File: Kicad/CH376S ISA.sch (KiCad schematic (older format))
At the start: 29 parts, among them J1 Bus_ISA_8bit, J2 ROM CS, J3 Conn_02x04_Odd_Even, U1 CH376, U13 74LS138, U14 74LS138, U15 74LS138, U2 LM1117-3.3, U3 74LS139, U4 74LS138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

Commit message: first draft done
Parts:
- removed C3: 0.1uF, Capacitor_THT:C_Disc_D4.3mm_W1.9mm_P5.00mm, symbol pspice:CAP
- removed J3: Conn_02x04_Odd_Even, Connector_PinHeader_2.54mm:PinHeader_2x04_P2.54mm_Vertical, symbol Connector_Generic:Conn_02x04_Odd_Even
- removed U3: 74LS139, Package_DIP:DIP-16_W7.62mm, symbol 74xx:74LS139
- removed U6: 28C64, Package_DIP:DIP-28_W15.24mm, symbol Memory_EPROM:27C64
- added U3: 28C256, Package_DIP:DIP-28_W15.24mm, symbol Memory_EEPROM:28C256
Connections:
- net IO_00EX is gone; now on net CH376CS: U15.7 (O7)
- net 5+: now also U3.28 (VCC)
- net A0: now also U3.10 (A0)
- net A1: now also U3.9 (A1)
- net A10: now also U3.21 (A10)
- net A11: now also U3.23 (A11)
- net A12: now also U3.2 (A12)
- net A2: now also U3.8 (A2)
- net A3: now also U3.7 (A3)
- net A4: now also U3.6 (A4)
- net A5: now also U3.5 (A5)
- net A6: now also U3.4 (A6)
- net A7: now also U3.3 (A7)
- net A8: now also U3.25 (A8)
- net A9: now also U3.24 (A9)
- net D0: now also U3.11 (D0)
- net D1: now also U3.12 (D1)
- net D2: now also U3.13 (D2)
- net D3: now also U3.15 (D3)
- net D4: now also U3.16 (D4)
- net D5: now also U3.17 (D5)
- net D6: now also U3.18 (D6)
- net D7: now also U3.19 (D7)
- net GND: now also U3.1 (A14), U3.14 (GND), U3.26 (A13); no longer U13.5 (E2), U4.5 (E2)
- net MRD: now also U3.22 (~OE)
- net MWR: now also U3.27 (~WE)
- net ROM_CS: now also U3.20 (~CS)
- net AEN: now reaches J1.42 (AEN)
- net AEN: now also U13.5 (E2), U4.5 (E2)
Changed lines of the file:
@@
 	1    0    0    -1
 $EndComp
-$Comp
-L 74xx:74LS139 U3
-U 1 1 642DE0FF
-P 13100 5525
-F 0 "U3" H 13100 5892 50  0000 C CNN
-F 1 "74LS139" H 13100 5801 50  0000 C CNN
-F 2 "Package_DIP:DIP-16_W7.62mm" H 13100 5525 50  0001 C CNN
-F 3 "http://www.ti.com/lit/ds/symlink/sn74ls139a.pdf" H 13100 5525 50  0001 C CNN
-	1    13100 5525
-	1    0    0    -1
-$EndComp
-$Comp
-L 74xx:74LS139 U3
-U 3 1 642DED85
-P 13100 6300
-F 0 "U3" V 12733 6300 50  0000 C CNN
-F 1 "74LS139" V 12824 6300 50  0000 C CNN
-F 2 "Package_DIP:DIP-16_W7.62mm" H 13100 6300 50  0001 C CNN
-F 3 "http://www.ti.com/lit/ds/symlink/sn74ls139a.pdf" H 13100 6300 50  0001 C CNN
-	3    13100 6300
-	0    1    1    0
-$EndComp
-Text Label 12600 6300 2    50   ~ 0
-GND
-Text Label 13600 6300 0    50   ~ 0
-5+
-Text Label 12600 5525 2    50   ~ 0
-A0
-Text Label 12600 5425 2    50   ~ 0
-A1
-Text Label 13600 5425 0    50   ~ 0
-E0
-Text Label 13600 5525 0    50   ~ 0
-E1
-Text Label 13600 5625 0    50   ~ 0
-E2
-Text Label 13600 5725 0    50   ~ 0
-E3
-Text Label 14325 5150 0    50   ~ 0
-GND
-Text Label 13825 5150 2    50   ~ 0
-5+
-$Comp
-L pspice:CAP C3
-U 1 1 642E2100
-P 14075 5150
-F 0 "C3" V 13760 5150 50  0000 C CNN
-F 1 "0.1uF" V 13851 5150 50  0000 C CNN
-F 2 "Capacitor_THT:C_Disc_D4.3mm_W1.9mm_P5.00mm" H 14075 5150 50  0001 C CNN
-F 3 "~" H 14075 5150 50  0001 C CNN
-	1    14075 5150
-	0    1    1    0
-$EndComp
-$Comp
-L Connector_Generic:Conn_02x04_Odd_Even J3
-U 1 1 642E381E
-P 14525 6625
-F 0 "J3" H 14575 6942 50  0000 C CNN
-F 1 "Conn_02x04_Odd_Even" H 14575 6851 50  0000 C CNN
-F 2 "Connector_PinHeader_2.54mm:PinHeader_2x04_P2.54mm_Vertical" H 14525 6625 50  0001 C CNN
-F 3 "~" H 14525 6625 50  0001 C CNN
-	1    14525 6625
-	1    0    0    -1
-$EndComp
-Text Label 14325 6525 2    50   ~ 0
-E0
-Text Label 14325 6625 2    50   ~ 0
-E1
-Text Label 14325 6725 2    50   ~ 0
-E2
-Text Label 14325 6825 2    50   ~ 0
-E3
 Text Label 14550 4125 0    50   ~ 0
-IO_00EX
-Text Label 12600 5725 2    50   ~ 0
-IO_00EX
-Text Label 14825 6525 0    50   ~ 0
-CH376CS
-Text Label 14825 6625 0    50   ~ 0
-CH376CS
-Text Label 14825 6725 0    50   ~ 0
-CH376CS
-Text Label 14825 6825 0    50   ~ 0
 CH376CS
 Text Label 6975 2725 0    50   ~ 0
@@
 Text Label 6475 3325 2    50   ~ 0
 A2
-Text Label 10175 3825 2    50   ~ 0
-GND
 $Comp
 L Connector:Bus_ISA_8bit J1
@@
 Text Label 12225 8525 0    50   ~ 0
 5+
-Text Label 11725 9425 2    50   ~ 0
-GND
 Text Label 14375 9825 0    50   ~ 0
 GND
@@
 	0    1    1    0
 $EndComp
-$Comp
-L Memory_EPROM:27C64 U6
-U 1 1 6434340C
-P 18775 9375
-F 0 "U6" H 18775 10556 50  0000 C CNN
-F 1 "28C64" H 18775 10465 50  0000 C CNN
-F 2 "Package_DIP:DIP-28_W15.24mm" H 18775 9375 50  0001 C CNN
-F 3 "http://ww1.microchip.com/downloads/en/DeviceDoc/11107M.pdf" H 18775 9375 50  0001 C CNN
-	1    18775 9375
-	1    0    0    -1
-$EndComp
-Text Label 18375 10175 2    50   ~ 0
-ROM_CS
-Text Label 18375 9975 2    50   ~ 0
+Text Label 17925 10175 2    50   ~ 0
+ROM_CS
+Text Label 17925 9975 2    50   ~ 0
 MWR
-Text Label 18375 10275 2    50   ~ 0
+Text Label 17925 10075 2    50   ~ 0
 MRD
-Text Label 18775 8375 2    50   ~ 0
-5+
-Text Label 18775 10475 0    50   ~ 0
-GND
-Text Label 18375 8575 2    50   ~ 0
+Text Label 18325 8175 2    50   ~ 0
+5+
+Text Label 18325 10375 0    50   ~ 0
+GND
+Text Label 17925 8375 2    50   ~ 0
 A0
-Text Label 18375 9775 2    50   ~ 0
+Text Label 17925 9575 2    50   ~ 0
 A12
-Text Label 18375 9675 2    50   ~ 0
+Text Label 17925 9475 2    50   ~ 0
 A11
-Text Label 18375 9575 2    50   ~ 0
+Text Label 17925 9375 2    50   ~ 0
 A10
-Text Label 18375 9475 2    50   ~ 0
+Text Label 17925 9275 2    50   ~ 0
 A9
-Text Label 18375 9375 2    50   ~ 0
+Text Label 17925 9175 2    50   ~ 0
 A8
-Text Label 18375 9275 2    50   ~ 0
+Text Label 17925 9075 2    50   ~ 0
 A7
-Text Label 18375 9175 2    50   ~ 0
+Text Label 17925 8975 2    50   ~ 0
 A6
-Text Label 18375 9075 2    50   ~ 0
+Text Label 17925 8875 2    50   ~ 0
 A5
-Text Label 18375 8975 2    50   ~ 0
+Text Label 17925 8775 2    50   ~ 0
 A4
-Text Label 18375 8875 2    50   ~ 0
+Text Label 17925 8675 2    50   ~ 0
 A3
-Text Label 18375 8775 2    50   ~ 0
+Text Label 17925 8575 2    50   ~ 0
 A2
-Text Label 18375 8675 2    50   ~ 0
+Text Label 17925 8475 2    50   ~ 0
 A1
-Text Label 19175 9275 0    50   ~ 0
+Text Label 18725 9075 0    50   ~ 0
 D7
-Text Label 19175 9175 0    50   ~ 0
+Text Label 18725 8975 0    50   ~ 0
 D6
-Text Label 19175 9075 0    50   ~ 0
+Text Label 18725 8875 0    50   ~ 0
 D5
-Text Label 19175 8975 0    50   ~ 0
+Text Label 18725 8775 0    50   ~ 0
 D4
-Text Label 19175 8775 0    50   ~ 0
+Text Label 18725 8575 0    50   ~ 0
 D2
-Text Label 19175 8875 0    50   ~ 0
+Text Label 18725 8675 0    50   ~ 0
 D3
-Text Label 19175 8675 0    50   ~ 0
+Text Label 18725 8475 0    50   ~ 0
 D1
-Text Label 19175 8575 0    50   ~ 0
+Text Label 18725 8375 0    50   ~ 0
 D0
 Text Label 19350 8100 0    50   ~ 0
@@
 	0    1    1    0
 $EndComp
+Text Label 10175 3825 2    50   ~ 0
+AEN
+Text Label 9050 9250 0    50   ~ 0
+AEN
+$Comp
+L Memory_EEPROM:28C256 U3
+U 1 1 64589300
+P 18325 9275
+F 0 "U3" H 18325 10556 50  0000 C CNN
+F 1 "28C256" H 18325 10465 50  0000 C CNN
+F 2 "Package_DIP:DIP-28_W15.24mm" H 18325 9275 50  0001 C CNN
+F 3 "http://ww1.microchip.com/downloads/en/DeviceDoc/doc0006.pdf" H 18325 9275 50  0001 C CNN
+	1    18325 9275
+	1    0    0    -1
+$EndComp
+Text Label 17925 9675 2    50   ~ 0
+GND
+Text Label 17925 9775 2    50   ~ 0
+GND
+Text Label 11725 9425 2    50   ~ 0
+AEN
 $EndSCHEMATC

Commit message: update
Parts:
- added J3: ROM CS, Connector_PinHeader_2.54mm:PinHeader_2x02_P2.54mm_Vertical, symbol Connector_Generic:Conn_02x02_Odd_Even
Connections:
- net 5+: no longer U5.6 (E3)
- net A16: now also U4.1 (A0); no longer U4.4 (E1)
- net A17: now also U4.2 (A1); no longer U4.1 (A0)
- net A18: now also U4.3 (A2); no longer U4.2 (A1)
- net A19: now also U5.6 (E3); no longer U4.3 (A2)
- net GND: now also U4.4 (E1)
- net ROM_CS_0XEX: now also U4.9 (O6), J3.3 (Pin_3); no longer U4.7 (O7), U5.4 (E1)
- net ROM_CS_0XDX: now reaches U4.10 (O5)
- net ROM_CS_0XDX: now also J3.1 (Pin_1)
- new net ROM_CS_E_D: J3.2 (Pin_2), J3.4 (Pin_4), U5.4 (E1)
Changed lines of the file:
@@
 Text Label 11725 9325 2    50   ~ 0
 REFQ
+Text Label 13875 9325 2    50   ~ 0
+A19
 Text Label 11725 9025 2    50   ~ 0
-A19
+A18
 Text Label 11725 8925 2    50   ~ 0
-A18
+A17
 Text Label 11725 8825 2    50   ~ 0
-A17
-Text Label 11725 9525 2    50   ~ 0
 A16
 Text Label 13875 9025 2    50   ~ 0
@@
 	1    0    0    -1
 $EndComp
-Text Label 12725 9525 0    50   ~ 0
-ROM_CS_0XEX
+Text Label 12925 10400 2    50   ~ 0
+ROM_CS_0XDX
 Text Label 12225 9825 0    50   ~ 0
 GND
@@
 GND
 Text Label 13875 9525 2    50   ~ 0
-ROM_CS_0XEX
+ROM_CS_E_D
 Text Label 13875 9425 2    50   ~ 0
 GND
-Text Label 13875 9325 2    50   ~ 0
-5+
 Text Label 14875 8825 0    50   ~ 0
 ROM_CS_0XE0
@@
 Text Label 11725 9425 2    50   ~ 0
 AEN
+Text Label 11725 9525 2    50   ~ 0
+GND
+$Comp
+L Connector_Generic:Conn_02x02_Odd_Even J3
+U 1 1 64733574
+P 13125 10400
+F 0 "J3" H 13175 10717 50  0000 C CNN
+F 1 "ROM CS" H 13175 10626 50  0000 C CNN
+F 2 "Connector_PinHeader_2.54mm:PinHeader_2x02_P2.54mm_Vertical" H 13125 10400 50  0001 C CNN
+F 3 "~" H 13125 10400 50  0001 C CNN
+	1    13125 10400
+	1    0    0    -1
+$EndComp
+Text Label 13425 10400 0    50   ~ 0
+ROM_CS_E_D
+Text Label 13425 10500 0    50   ~ 0
+ROM_CS_E_D
+Text Label 12925 10500 2    50   ~ 0
+ROM_CS_0XEX
+Text Label 12725 9325 0    50   ~ 0
+ROM_CS_0XDX
+Text Label 12725 9425 0    50   ~ 0
+ROM_CS_0XEX
 $EndSCHEMATC

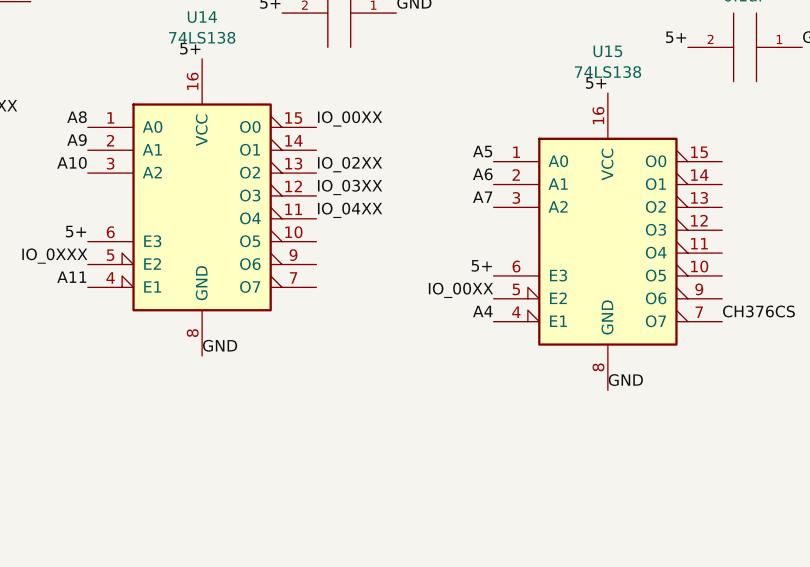
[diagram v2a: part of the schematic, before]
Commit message: Changed IO address to 0x07E0
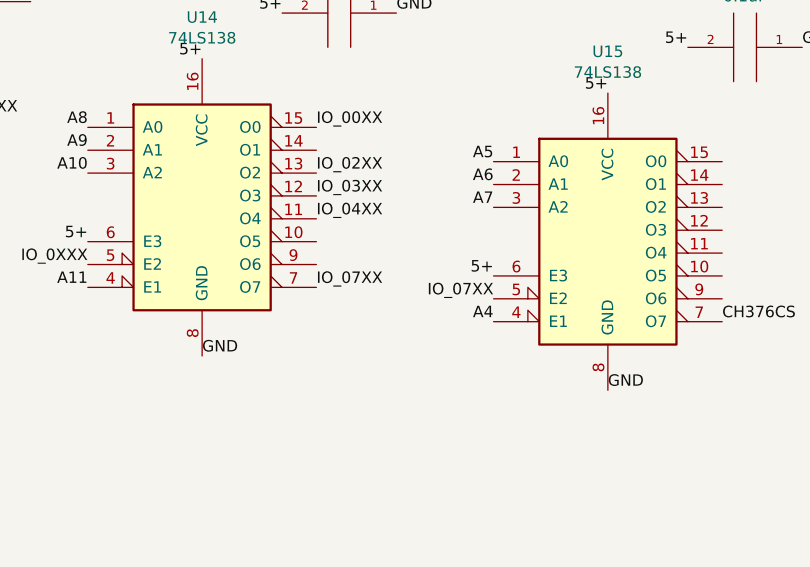
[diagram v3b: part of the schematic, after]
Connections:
- net IO_00XX: no longer U15.5 (E2)
- net IO_07XX: now reaches U14.7 (O7)
- net IO_07XX: now also U15.5 (E2)
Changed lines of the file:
@@
 Text Label 13550 4125 2    50   ~ 0
 A4
-Text Label 13550 4025 2    50   ~ 0
-IO_00XX
 Text Label 14050 3125 2    50   ~ 0
 5+
@@
 Text Label 12725 9425 0    50   ~ 0
 ROM_CS_0XEX
+Text Label 12775 3975 0    50   ~ 0
+IO_07XX
+Text Label 13550 4025 2    50   ~ 0
+IO_07XX
 $EndSCHEMATC
